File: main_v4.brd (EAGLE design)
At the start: 88.6 x 33 mm, 23 parts, among them U1 CD4026B_N_16, U2 CD4026B_N_16

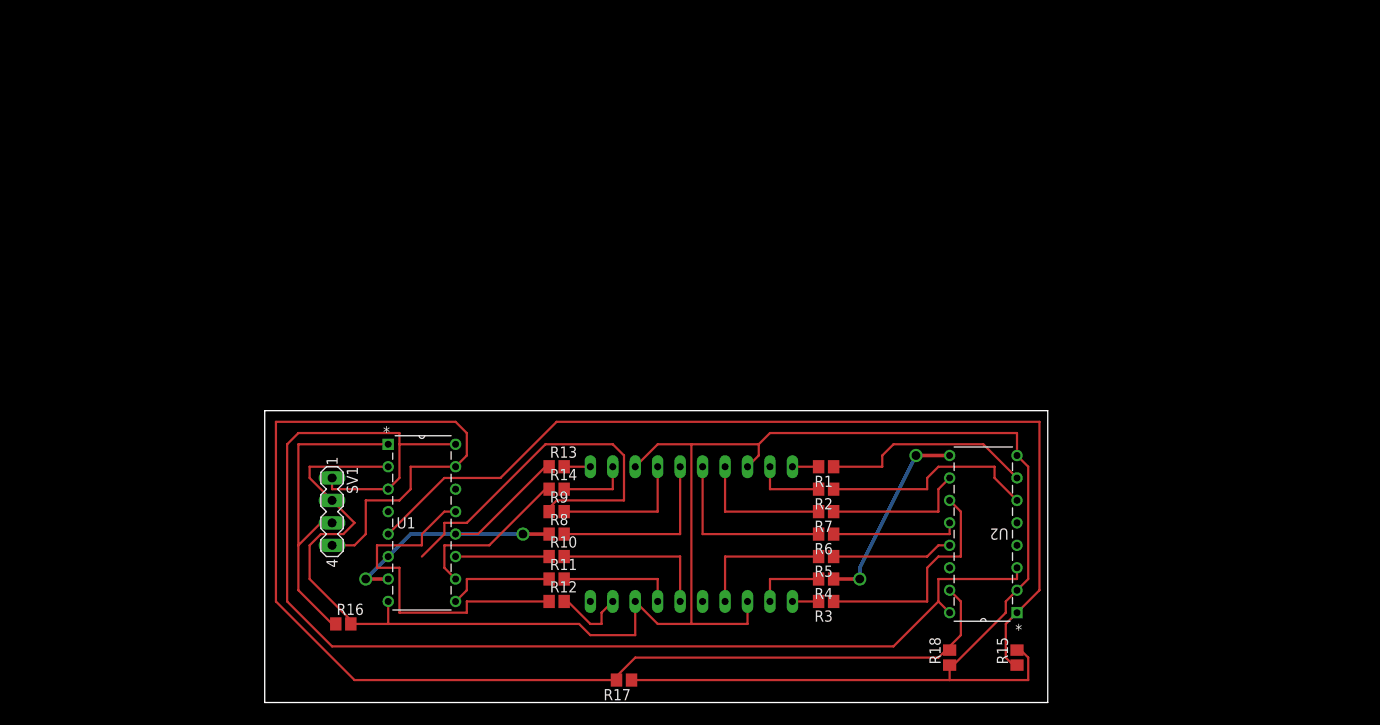
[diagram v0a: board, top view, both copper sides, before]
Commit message: Add v4 mirror drivers
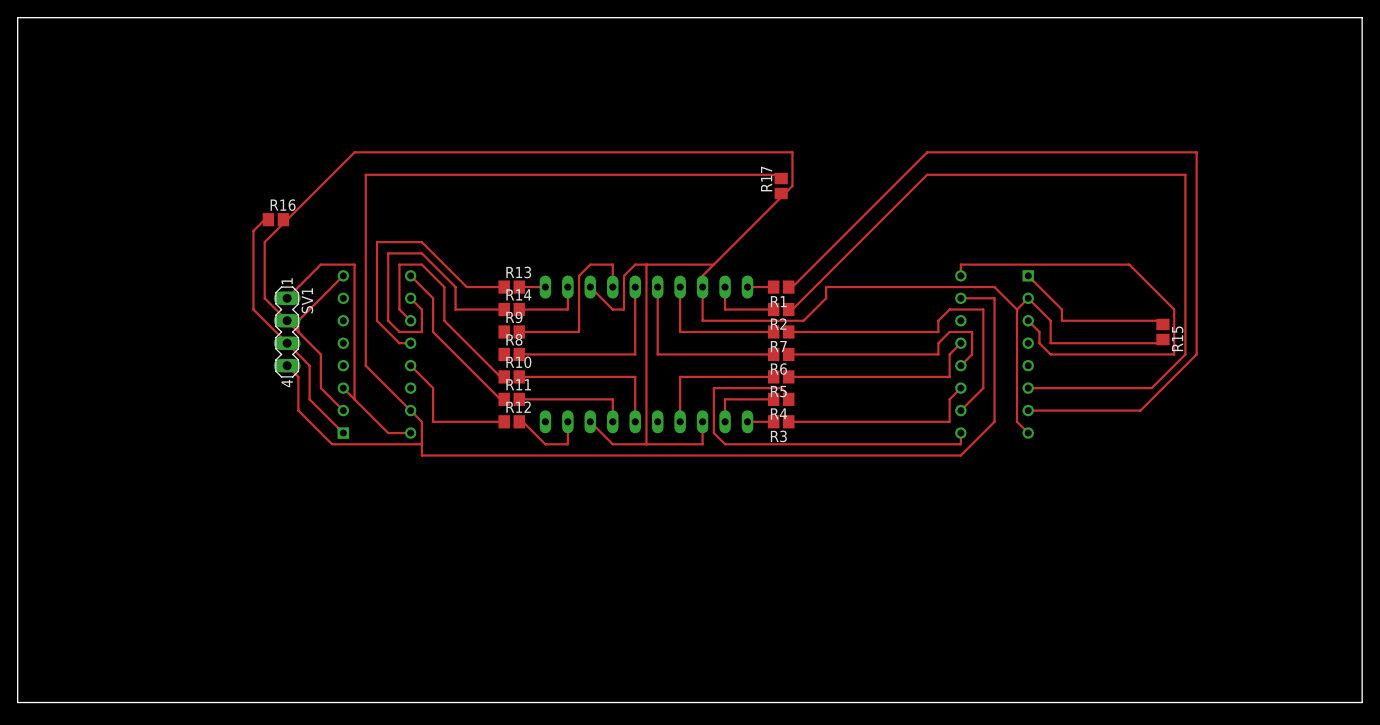
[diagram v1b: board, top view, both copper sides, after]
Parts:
- removed R18: 10K, resistor:R0805
- moved R17 58.6 mm to (58.4, 58.4), turned to 90 degrees
- moved R16 46.4 mm to (1.27, 54.6)
- moved R15 40.4 mm to (101.6, 41.9), turned to 270 degrees
- moved U1 37.2 mm to (16.5, 48.3), flipped to the bottom, turned to 180 degrees
- moved R14 20.9 mm to (27.9, 44.5)
- moved R2 20.9 mm to (58.4, 44.5)
- moved R1 20.9 mm to (58.4, 47.0)
- moved R11 20.9 mm to (27.9, 34.3)
- moved R12 20.9 mm to (27.9, 31.8)
- moved R13 20.9 mm to (27.9, 47.0)
- moved R3 20.9 mm to (58.4, 31.8)
- moved R4 20.9 mm to (58.4, 34.3)
- moved LED1 20.9 mm to (36.8, 39.4)
- moved LED2 20.9 mm to (49.5, 39.4)
- moved R10 20.9 mm to (27.9, 36.8)
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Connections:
- removed net N$26: R17.2, R18.2, SV1.4, U1.15, U2.15
- new net N$20: R17.2, SV1.4, U1.15, U2.15
- net N$9: no longer R18.1
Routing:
- net N$20: track 0.00 -> 187.1 mm
- net N$26: track 157.8 -> 0.00 mm
- net N$27: track 109.4 -> 18.5 mm
- net N$25: track 24.1 -> 97.0 mm
- net N$24: track 24.9 -> 90.9 mm
- net N$8: track 144.2 -> 85.6 mm
- net N$28: track 44.3 -> 0.00 mm
- net N$29: track 25.4 -> 0.00 mm, vias 2 -> 0
- net N$30: track 39.6 -> 15.4 mm
- net N$22: track 22.2 -> 44.7 mm, vias 2 -> 0
- net N$18: track 16.2 -> 36.3 mm
- net N$31: track 13.7 -> 30.2 mm
- net N$32: track 10.6 -> 26.2 mm
- net N$33: track 18.8 -> 33.5 mm
- net N$19: track 14.4 -> 26.9 mm
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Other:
- board size 88.6 x 33 mm -> 152.1 x 77.5 mm
